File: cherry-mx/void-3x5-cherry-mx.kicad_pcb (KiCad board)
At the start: 2 copper layers, 140.5 x 112.5 mm, 81 parts, among them J1 Conn_01x02, J2 Conn_01x03_MountingPin, J3 Conn_01x02

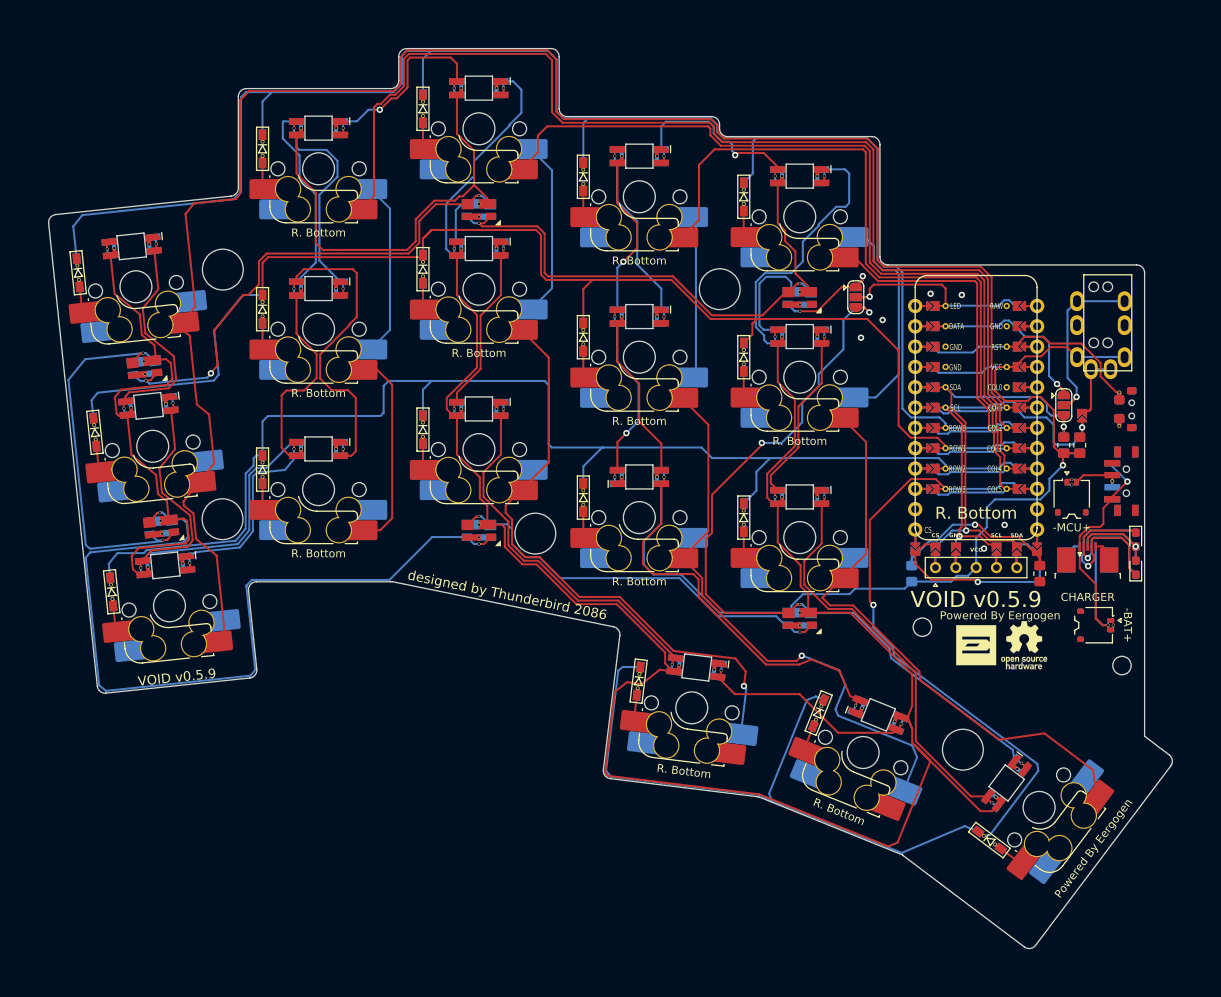
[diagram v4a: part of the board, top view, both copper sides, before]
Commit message: updated cherry-mx
usb-c for communication between left and right hand sides
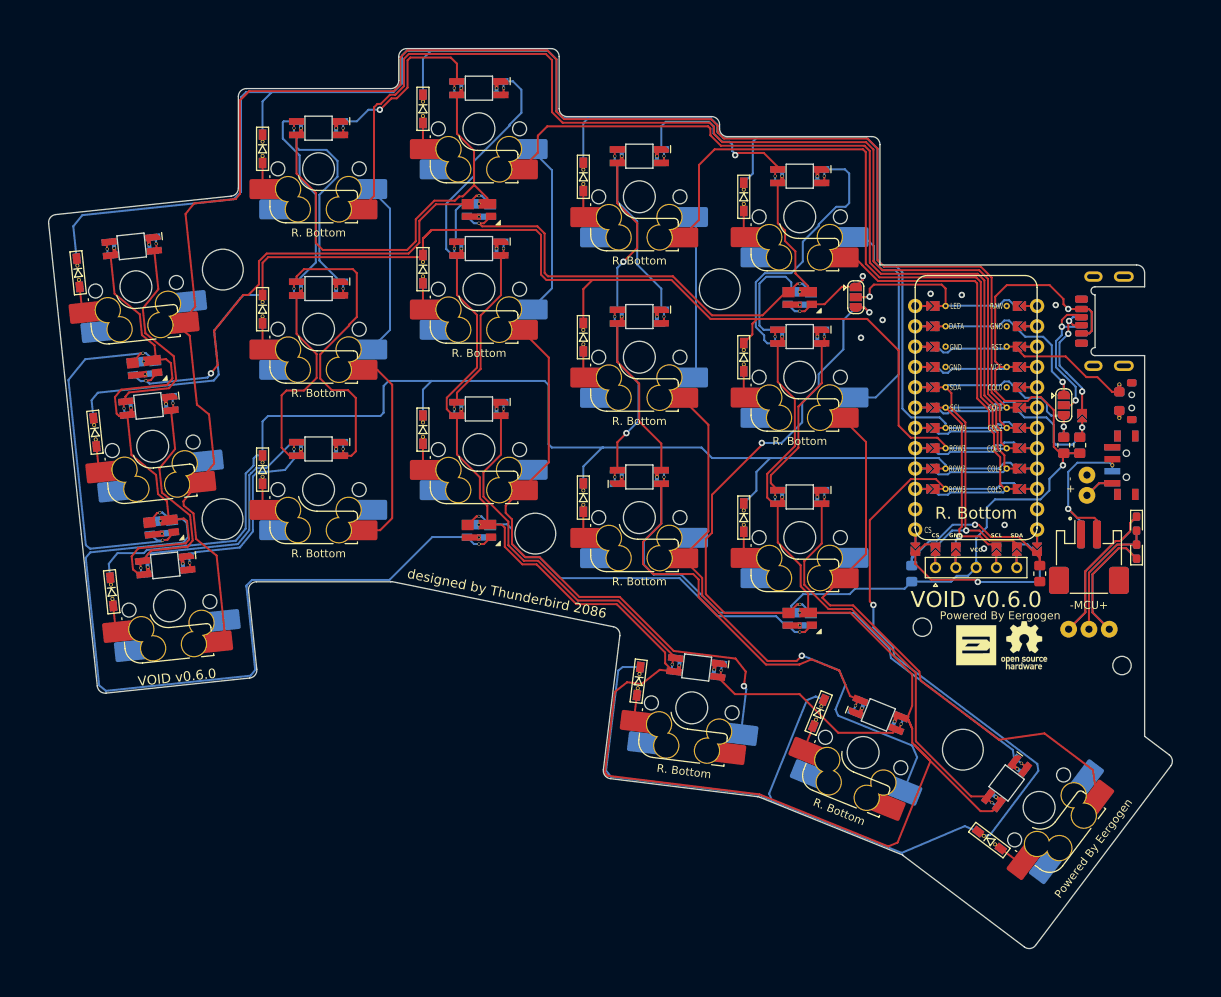
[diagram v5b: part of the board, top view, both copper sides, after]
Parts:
- removed TRRS1: MJ-4PP-9, TB2086_MISC:TRRS-PJ-320A-rev
- added J4: Conn_01x03, TB2086_MISC:Pogopin_1x03_P2.54mm, F.Cu at (210.9, 112.9)
- added SW_SPDT2: SW_SPDT2, TB2086_SMD:SW_SPDT_PCM12, F.Cu at (215.3, 92.4)
- J1: value Conn_01x02 -> USB_C_Receptacle_PowerOnly_6P; footprint TB2086_MISC:Molex_Pico-EZmate_78171-0002_1x02-1MP_P1.20mm_Vertical_rev -> TB2086_SMD:USB-20C-F-6C16_rev
- J2: value Conn_01x03_MountingPin -> Conn_01x02; footprint TB2086_MISC:TE_0-1734839-5_1x05-1MP_P0.5mm_Horizontal-rev -> TB2086_SMD:JST_PH_S2B-PH-SM4-TB_1x02-1MP_P2.00mm_Horizontal_rev
- J3: footprint TB2086_MISC:Molex_Pico-EZmate_78171-0002_1x02-1MP_P1.20mm_Vertical_rev -> TB2086_MISC:Pogopin_1x02_P2.54mm; moved to F.Cu
- L19, L20, L21, L22, L23, L24: footprint LED_SK6812MINI_PLCC4_3.5x3.5mm_P1.75mm_rev_all -> TB2086_LED:LED_SK6812MINI_PLCC4_3.5x3.5mm_P1.75mm_rev_all; moved to F.Cu
- LED1, LED2, LED3, LED4: footprint TB2086_SMD:LED_0603_1608Metric_Pad1.05x0.95mm_HandSolder -> TB2086_LED:LED_0603_1608Metric_Pad1.05x0.95mm_HandSolder
- R1: footprint R_0805_2012Metric_Pad1.20x1.40mm_HandSolder -> Resistor_SMD:R_0805_2012Metric_Pad1.20x1.40mm_HandSolder; moved to B.Cu
- R2: footprint R_0805_2012Metric_Pad1.20x1.40mm_HandSolder -> Resistor_SMD:R_0805_2012Metric_Pad1.20x1.40mm_HandSolder
- SW_SPDT1: value SW_SPDT -> SW_SPDT1; footprint TB2086_SMD:SW_SPDT_PCM12_reversible -> TB2086_SMD:SW_SPDT_PCM12
- moved J1 22.7 mm to (214.5, 74.4), turned to 90 degrees
- moved J3 17.5 mm to (210.7, 94.9), turned to -90 degrees
- moved LED1 5.50 mm to (216.9, 99.7), turned to -90 degrees
- moved LED2 2.00 mm to (216.9, 99.7)
- moved LED3 2.00 mm to (216.9, 103.2), turned to 90 degrees
- moved SW_SPDT1 2.00 mm to (215.3, 92.4)
- moved LED4 1.50 mm to (216.9, 103.2)
- moved RSW1 1.00 mm to (216.3, 84.4)
- moved J2 0.15 mm to (210.9, 103.9)
- turned L24 to 0 degrees
- turned L20 to 0 degrees
- turned L23 to 0 degrees
- turned L21 to 6 degrees
- turned L22 to 6 degrees
- turned L19 to 0 degrees
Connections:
- J2 pad 1: BAT -> GND
- JP2 pad 2: Net-(JP2-C) -> Net-(J1-CC2)
- JP3 pad 2: Net-(JP3-B) -> Net-(J1-CC1)
- LED1 pad 1: Net-(J2-Pin_4) -> Net-(J4-Pin_1)
- LED1 pad 2: Net-(J2-Pin_3) -> Net-(J4-Pin_2)
- LED2 pad 1: Net-(J2-Pin_4) -> Net-(J4-Pin_1)
- LED2 pad 2: Net-(J2-Pin_3) -> Net-(J4-Pin_2)
- LED3 pad 1: Net-(J2-Pin_2) -> Net-(J4-Pin_3)
- LED3 pad 2: Net-(J2-Pin_3) -> Net-(J4-Pin_2)
- LED4 pad 1: Net-(J2-Pin_2) -> Net-(J4-Pin_3)
- LED4 pad 2: Net-(J2-Pin_3) -> Net-(J4-Pin_2)
- SW_SPDT1 pad 2: Net-(J1-Pin_2) -> Net-(J2-Pin_2)
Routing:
- net Net-(J4-Pin_1): track 0.00 -> 35.9 mm
- net Net-(J4-Pin_2): track 0.00 -> 32.4 mm
- net Net-(J4-Pin_3): track 0.00 -> 30.2 mm
- net BAT: track 37.1 -> 7.60 mm, vias 1 -> 0
- net Net-(J2-Pin_4): track 23.9 -> 0.00 mm, vias 1 -> 0
- net Net-(JP2-C): track 22.9 -> 0.00 mm, vias 1 -> 0
- net Net-(J1-CC2): track 0.00 -> 20.2 mm, vias 0 -> 2
- net VCC: track 627.6 -> 646.9 mm, vias 2 -> 3
- net Net-(J2-Pin_3): track 19.3 -> 0.00 mm, vias 1 -> 0
- net Net-(J1-CC1): track 0.00 -> 19.1 mm, vias 0 -> 3
- net Net-(JP3-B): track 14.8 -> 0.00 mm
- net GND: track 5.73 -> 0.00 mm, vias 6 -> 7
- net Net-(J1-Pin_2): track 4.83 -> 0.00 mm
- net RESET: track 28.1 -> 25.7 mm
- net Net-(J2-Pin_2): track 21.5 -> 20.5 mm
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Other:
- outline, holes or cut-outs redrawn
- board text added: "- +"
- board text added: "VOID v0.6.0"
- board text removed: "-BAT+"
- board text removed: "CHARGER"
- board text removed: "VOID v0.5.9"

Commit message: updated choc
* fixed corner
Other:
- outline, holes or cut-outs redrawn
- board text added: "This corner was manually created."
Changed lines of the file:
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@@
 		(fp_arc
 			(start 4.085176 -6.75022)
-			(mid 5.499389 -6.164434)
+			(mid 5.499392 -6.164435)
 			(end 6.085176 -4.75022)
 			(stroke
@@
 		(fp_arc
 			(start 4.085176 -6.75022)
-			(mid 5.499389 -6.164434)
+			(mid 5.499392 -6.164435)
 			(end 6.085176 -4.75022)
 			(stroke
@@
 		(fp_arc
 			(start 4.085176 -6.75022)
-			(mid 5.499389 -6.164434)
+			(mid 5.499392 -6.164435)
 			(end 6.085176 -4.75022)
 			(stroke
@@
 		(fp_arc
 			(start 4.085176 -6.75022)
-			(mid 5.499389 -6.164434)
+			(mid 5.499392 -6.164435)
 			(end 6.085176 -4.75022)
 			(stroke
@@
 		(fp_arc
 			(start 4.085176 -6.75022)
-			(mid 5.499389 -6.164434)
+			(mid 5.499392 -6.164435)
 			(end 6.085176 -4.75022)
 			(stroke
@@
 		(fp_arc
 			(start 4.085176 -6.75022)
-			(mid 5.499389 -6.164434)
+			(mid 5.499392 -6.164435)
 			(end 6.085176 -4.75022)
 			(stroke
@@
 		(fp_arc
 			(start 4.085176 -6.75022)
-			(mid 5.499389 -6.164434)
+			(mid 5.499392 -6.164435)
 			(end 6.085176 -4.75022)
 			(stroke
@@
 		(fp_arc
 			(start 4.085176 -6.75022)
-			(mid 5.499389 -6.164434)
+			(mid 5.499392 -6.164435)
 			(end 6.085176 -4.75022)
 			(stroke
@@
 		(fp_arc
 			(start -2.444146 -0.85)
-			(mid -1.620516 -2.173416)
+			(mid -1.620517 -2.173415)
 			(end -0.149824 -2.69)
 			(stroke
@@
 		(fp_arc
 			(start 4.085176 -6.75022)
-			(mid 5.499389 -6.164435)
+			(mid 5.499392 -6.164435)
 			(end 6.085176 -4.75022)
 			(stroke
@@
 		(fp_line
 			(start 7.465 -6.31)
-			(end 4.915002 -6.31)
+			(end 4.915003 -6.31)
 			(stroke
 				(width 0.05)
@@
 		(fp_line
 			(start 4.915 -6.74)
-			(end 4.915002 -6.31)
+			(end 4.915003 -6.31)
 			(stroke
 				(width 0.05)
@@
 		(fp_arc
 			(start 4.085176 -6.75022)
-			(mid 5.499389 -6.164435)
+			(mid 5.499392 -6.164435)
 			(end 6.085176 -4.75022)
 			(stroke
@@
 		(fp_arc
 			(start 4.085176 -6.75022)
-			(mid 5.499389 -6.164434)
+			(mid 5.499392 -6.164435)
 			(end 6.085176 -4.75022)
 			(stroke
@@
 		(fp_arc
 			(start 4.085176 -6.75022)
-			(mid 5.499389 -6.164434)
+			(mid 5.499392 -6.164435)
 			(end 6.085176 -4.75022)
 			(stroke
@@
 		(at 154.701652 93.830424 180)
 		(property "Reference" "L10"
-			(at 0 2.1 360)
+			(at 0 2.1 0)
 			(layer "Eco1.User")
 			(effects
@@
 		)
 		(property "Value" "SK6812MINI-E"
-			(at 0 -0.5 360)
+			(at 0 -0.5 0)
 			(layer "B.SilkS")
 			(hide yes)
@@
 		)
 		(property "Footprint" "TB2086_LED:LED_SK6812MINI-E_rev"
-			(at 0 0 360)
+			(at 0 0 0)
 			(layer "F.Fab")
 			(hide yes)
@@
 		)
 		(property "Datasheet" "https://cdn-shop.adafruit.com/product-files/2686/SK6812MINI_REV.01-1-2.pdf"
-			(at 0 0 360)
+			(at 0 0 0)
 			(layer "F.Fab")
 			(hide yes)
@@
 		)
 		(property "Description" ""
-			(at 0 0 360)
+			(at 0 0 0)
 			(layer "F.Fab")
 			(hide yes)
@@
 		(fp_arc
 			(start 4.085176 -6.75022)
-			(mid 5.499389 -6.164434)
+			(mid 5.499392 -6.164435)
 			(end 6.085176 -4.75022)
 			(stroke
@@
 		(fp_arc
 			(start 4.085176 -6.75022)
-			(mid 5.499389 -6.164434)
+			(mid 5.499392 -6.164435)
 			(end 6.085176 -4.75022)
 			(stroke
@@
 		(fp_arc
 			(start 4.085176 -6.75022)
-			(mid 5.499389 -6.164434)
+			(mid 5.499392 -6.164435)
 			(end 6.085176 -4.75022)
 			(stroke
@@
 		(fp_arc
 			(start 4.085176 -6.75022)
-			(mid 5.499389 -6.164434)
+			(mid 5.499392 -6.164435)
 			(end 6.085176 -4.75022)
 			(stroke
@@
 		(fp_arc
 			(start 4.085176 -6.75022)
-			(mid 5.499389 -6.164434)
+			(mid 5.499392 -6.164435)
 			(end 6.085176 -4.75022)
 			(stroke
@@
 		(fp_arc
 			(start 4.085176 -6.75022)
-			(mid 5.499389 -6.164434)
+			(mid 5.499392 -6.164435)
 			(end 6.085176 -4.75022)
 			(stroke
@@
 		)
 		(pad "1" thru_hole circle
-			(at -2.200002 0 353)
+			(at -2.200003 0 353)
 			(size 0.4 0.4)
 			(drill 0.3)
@@
 		)
 		(pad "3" thru_hole circle
-			(at 2.200002 0 353)
+			(at 2.200003 0 353)
 			(size 0.4 0.4)
 			(drill 0.3)
@@
 		(fp_arc
 			(start 4.085176 -6.75022)
-			(mid 5.499389 -6.164434)
+			(mid 5.499392 -6.164435)
 			(end 6.085176 -4.75022)
 			(stroke
@@
 		(fp_arc
 			(start 4.085176 -6.75022)
-			(mid 5.499389 -6.164434)
+			(mid 5.499392 -6.164435)
 			(end 6.085176 -4.75022)
 			(stroke
@@
 		(fp_arc
 			(start 4.085176 -6.75022)
-			(mid 5.499389 -6.164434)
+			(mid 5.499392 -6.164435)
 			(end 6.085176 -4.75022)
 			(stroke
@@
 		(fp_arc
 			(start 4.085176 -6.75022)
-			(mid 5.499389 -6.164434)
+			(mid 5.499392 -6.164435)
 			(end 6.085176 -4.75022)
 			(stroke
@@
 		(fp_arc
 			(start 4.085176 -6.75022)
-			(mid 5.499389 -6.164434)
+			(mid 5.499392 -6.164435)
 			(end 6.085176 -4.75022)
 			(stroke
@@
 		(fp_arc
 			(start 4.085176 -6.75022)
-			(mid 5.499389 -6.164434)
+			(mid 5.499392 -6.164435)
 			(end 6.085176 -4.75022)
 			(stroke
@@
 		(fp_arc
 			(start -2.444146 -0.85)
-			(mid -1.620516 -2.173416)
+			(mid -1.620517 -2.173415)
 			(end -0.149824 -2.69)
 			(stroke
@@
 		(fp_arc
 			(start 4.085176 -6.75022)
-			(mid 5.499389 -6.164435)
+			(mid 5.499392 -6.164435)
 			(end 6.085176 -4.75022)
 			(stroke
@@
 		(fp_line
 			(start 7.465 -6.31)
-			(end 4.915002 -6.31)
+			(end 4.915003 -6.31)
 			(stroke
 				(width 0.05)
@@
 		(fp_line
 			(start 4.915 -6.74)
-			(end 4.915002 -6.31)
+			(end 4.915003 -6.31)
 			(stroke
 				(width 0.05)
@@
 		(fp_arc
 			(start 4.085176 -6.75022)
-			(mid 5.499389 -6.164435)
+			(mid 5.499392 -6.164435)
 			(end 6.085176 -4.75022)
 			(stroke
@@
 		(fp_arc
 			(start 4.864824 -3.20022)
-			(mid 4.718377 -2.846668)
+			(mid 4.718378 -2.846665)
 			(end 4.364824 -2.70022)
 			(stroke
@@
 		(fp_arc
 			(start 4.085176 -6.75022)
-			(mid 5.499388 -6.164435)
+			(mid 5.499392 -6.164435)
 			(end 6.085176 -4.75022)
 			(stroke
@@
 		(fp_arc
 			(start 4.085176 -6.75022)
-			(mid 5.499388 -6.164435)
+			(mid 5.499392 -6.164435)
 			(end 6.085176 -4.75022)
 			(stroke
@@
 		(fp_arc
 			(start -6.035 -4.74)
-			(mid -5.449215 -6.154216)
+			(mid -5.449215 -6.154215)
 			(end -4.035 -6.74)
 			(stroke
@@
 		(fp_arc
 			(start 4.085176 -6.75022)
-			(mid 5.499388 -6.164435)
+			(mid 5.499393 -6.164435)
 			(end 6.085176 -4.75022)
 			(stroke
@@
 		(fp_arc
 			(start -2.444146 -0.85)
-			(mid -1.620326 -2.173179)
+			(mid -1.620327 -2.173178)
 			(end -0.149824 -2.69)
 			(stroke
@@
 		(fp_arc
 			(start -6.035 -4.74)
-			(mid -5.449215 -6.154216)
+			(mid -5.449215 -6.154215)
 			(end -4.035 -6.74)
 			(stroke
@@
 		(fp_arc
 			(start 4.085176 -6.75022)
-			(mid 5.499388 -6.164435)
+			(mid 5.499393 -6.164435)
 			(end 6.085176 -4.75022)
 			(stroke
@@
 		(fp_arc
 			(start 4.085176 -6.75022)
-			(mid 5.499389 -6.164434)
+			(mid 5.499392 -6.164435)
 			(end 6.085176 -4.75022)
 			(stroke
@@
 		(fp_arc
 			(start 4.085176 -6.75022)
-			(mid 5.499389 -6.164434)
+			(mid 5.499392 -6.164435)
 			(end 6.085176 -4.75022)
 			(stroke
@@
 		(fp_arc
 			(start -2.444146 -0.85)
-			(mid -1.620516 -2.173416)
+			(mid -1.620517 -2.173415)
 			(end -0.149824 -2.69)
 			(stroke
@@
 		(fp_arc
 			(start 4.085176 -6.75022)
-			(mid 5.499389 -6.164435)
+			(mid 5.499392 -6.164435)
 			(end 6.085176 -4.75022)
 			(stroke
@@
 		(fp_line
 			(start 7.465 -6.31)
-			(end 4.915002 -6.31)
+			(end 4.915003 -6.31)
 			(stroke
 				(width 0.05)
@@
 		(fp_line
 			(start 4.915 -6.74)
-			(end 4.915002 -6.31)
+			(end 4.915003 -6.31)
 			(stroke
 				(width 0.05)
@@
 		(fp_arc
 			(start 4.085176 -6.75022)
-			(mid 5.499389 -6.164435)
+			(mid 5.499392 -6.164435)
 			(end 6.085176 -4.75022)
 			(stroke
@@
 		(fp_arc
 			(start 4.085176 -6.75022)
-			(mid 5.499389 -6.164434)
+			(mid 5.499392 -6.164435)
 			(end 6.085176 -4.75022)
 			(stroke
@@
 		(fp_arc
 			(start 4.085176 -6.75022)
-			(mid 5.499389 -6.164434)
+			(mid 5.499392 -6.164435)
 			(end 6.085176 -4.75022)
 			(stroke
@@
 		(tags "resistor handsolder")
 		(property "Reference" "R2"
-			(at 0 -1.65 270)
+			(at 0 -1.65 -90)
 			(layer "F.SilkS")
 			(hide yes)
@@
 	(gr_line
 		(start 216.859152 67.325424)
-		(end 184.776652 67.325424)
+		(end 186.130111 67.316187)
 		(stroke
 			(width 0.15)
@@
 	)
 	(gr_arc
+		(start 186.130111 67.316187)
+		(mid 185.178102 66.921898)
+		(end 184.783813 65.969889)
+		(stroke
+			(width 0.15)
+			(type default)
+		)
+		(layer "Edge.Cuts")
+	)
+	(gr_arc
 		(start 123.811084 106.918269)
 		(mid 123.719266 106.931122)
@@
 	)
 	(gr_line
-		(start 184.776652 67.325424)
+		(start 184.783813 65.969889)
 		(end 184.776652 52.285424)
 		(stroke
@@
 		)
 	)
+	(gr_text "This corner was manually created. "
+		(at 185.7681 66.1319 0)
+		(layer "Cmts.User")
+		(effects
+			(font
+				(size 1 1)
+				(thickness 0.15)
+			)
+			(justify left bottom)
+		)
+	)
